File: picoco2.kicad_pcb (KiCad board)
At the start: 2 copper layers, 54 x 102.9 mm, 40 parts, among them J1 Conn_01x03_Female, J2 Micro_SD_Card, J3 Conn_01x03_Female, Q1 Q_NMOS_GDS, SW1 SW_Push, SW2 SW_Push, U1 PicoW, U2 scd30, U3 ssd1306, U4 PCF8523T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

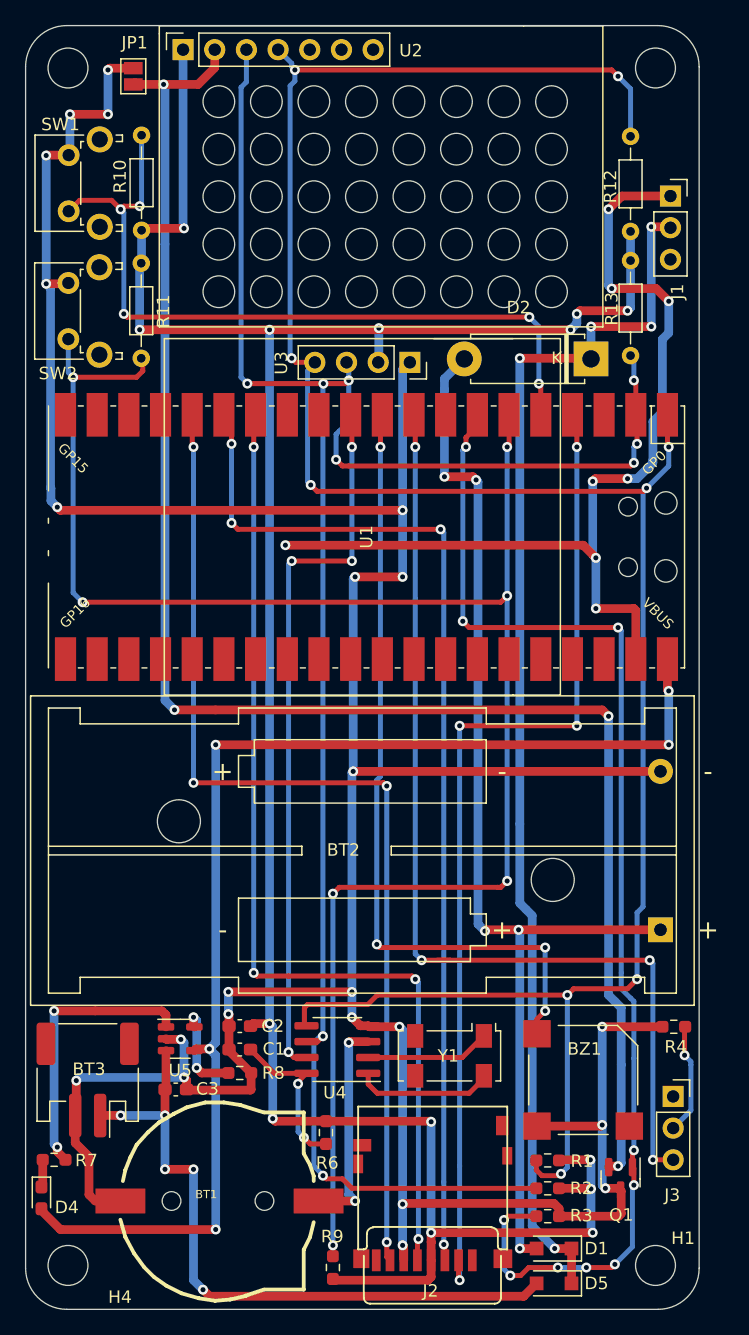
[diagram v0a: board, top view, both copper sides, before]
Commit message: fully routed
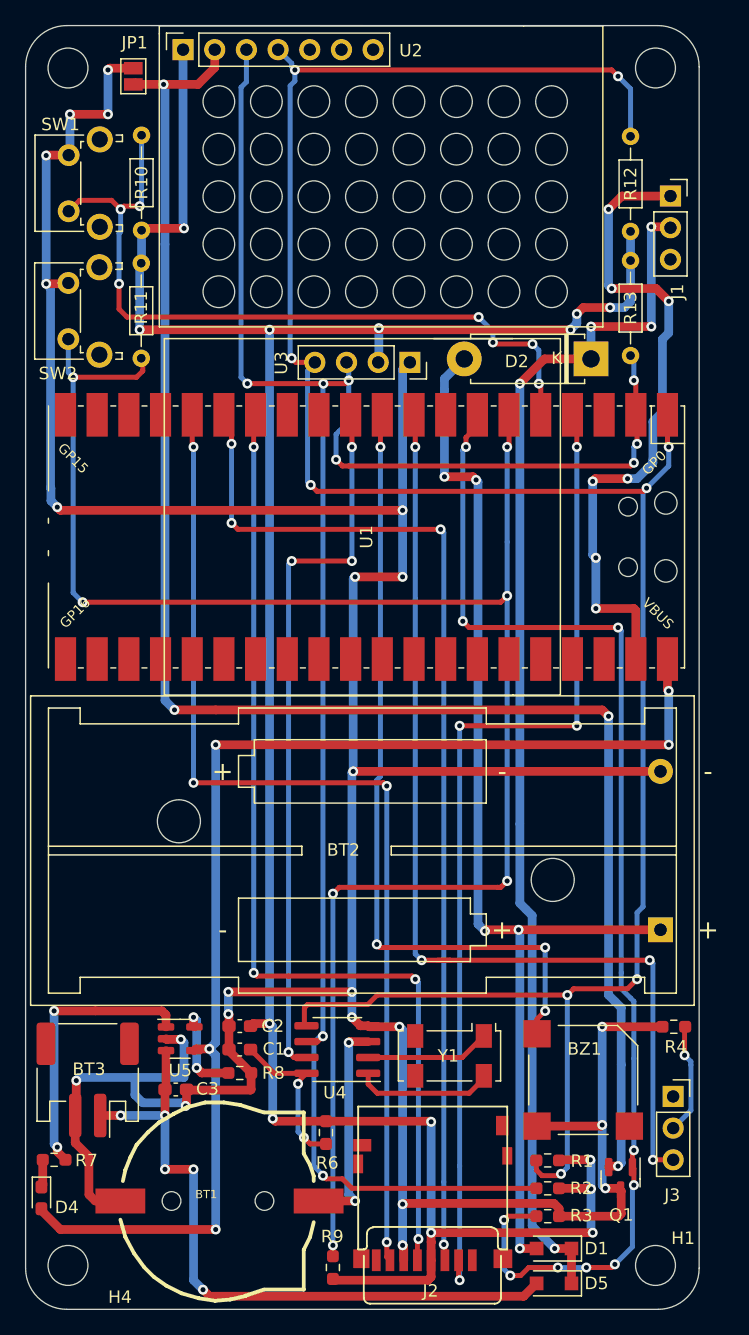
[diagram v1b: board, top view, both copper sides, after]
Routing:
- net VSYS: track 77.7 -> 52.4 mm, vias 8 -> 7
- net GND: track 271.2 -> 277.4 mm
- net Net-(D1-Pad1): track 99.4 -> 98.2 mm
- net BUT_A: track 62.4 -> 61.9 mm, vias 5 -> 7

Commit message: fully routed, revised ssd1306 display module
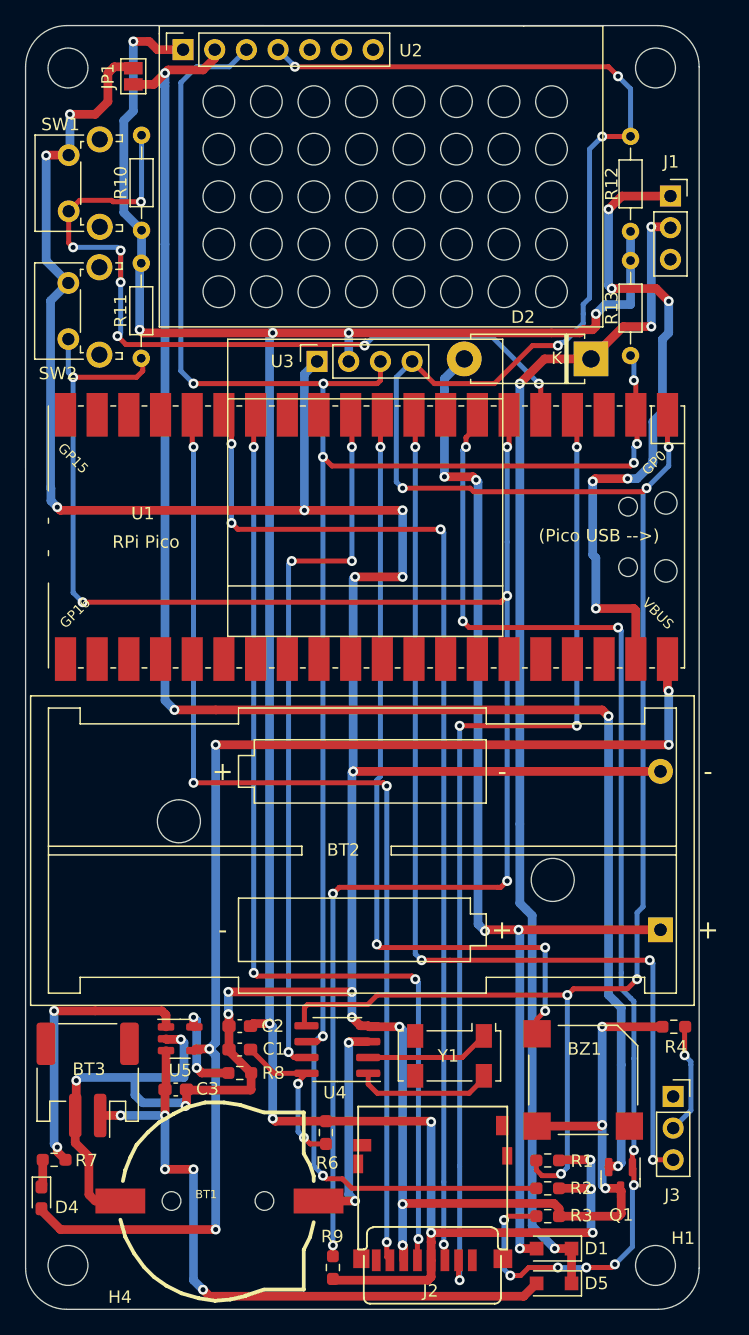
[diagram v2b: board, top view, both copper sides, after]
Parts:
- moved U3 7.44 mm to (23.4, 26.9), turned to 90 degrees
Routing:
- net BUT_A: track 61.9 -> 67.5 mm
- net SCL: track 160.1 -> 165.4 mm, vias 9 -> 8
- net +3V3: track 197.5 -> 200.2 mm, vias 14 -> 12
- net SDA: track 188.4 -> 190.5 mm, vias 9 -> 10
- net Net-(D1-Pad1): track 98.2 -> 96.7 mm, vias 5 -> 4
- net WRITE_EN: track 80.1 -> 79.1 mm
- net GND: track 277.4 -> 276.5 mm, vias 23 -> 21
- net SCD30_GND: track 131.9 -> 132.4 mm
- net VSYS: vias 7 -> 6
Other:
- board text added: "(Pico USB -->)"
- board text added: "RPi Pico"

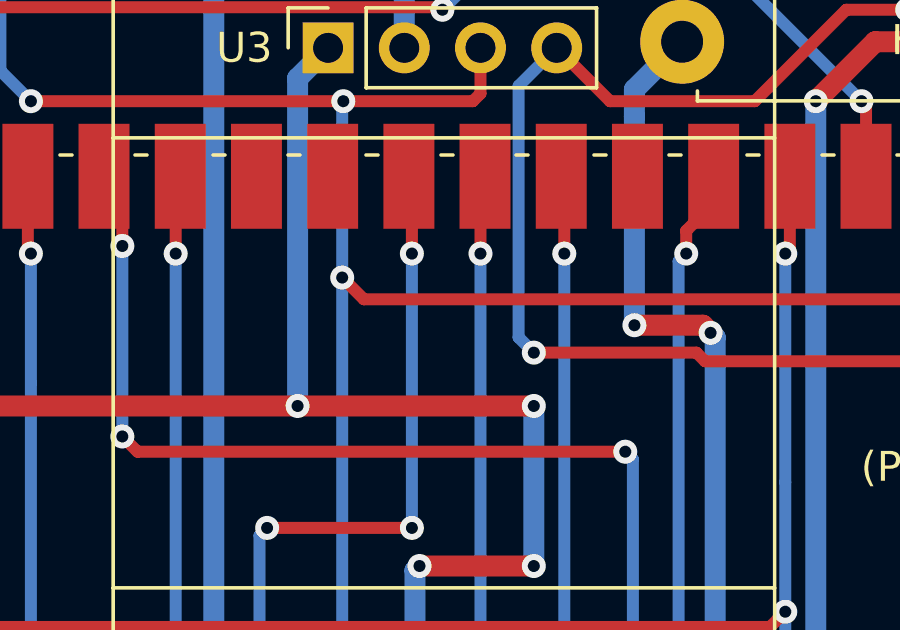
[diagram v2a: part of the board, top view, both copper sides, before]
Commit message: added label for ssd1306
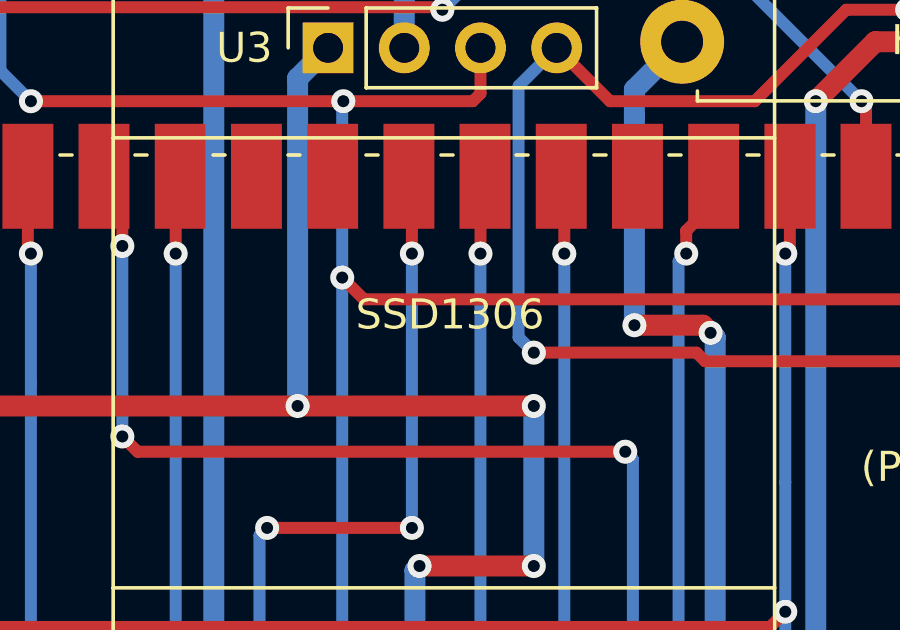
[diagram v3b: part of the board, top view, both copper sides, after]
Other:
- board text added: "SSD1306"
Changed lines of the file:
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@@
+    (effects (font (size 1 1) (thickness 0.15)))
+  )
+  (gr_text "SSD1306" (at 27.432 35.814) (layer "F.SilkS")
     (effects (font (size 1 1) (thickness 0.15)))
   )
